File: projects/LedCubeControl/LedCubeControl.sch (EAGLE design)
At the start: 20 parts, among them IC1 74HC595N, IC2 74HC595N

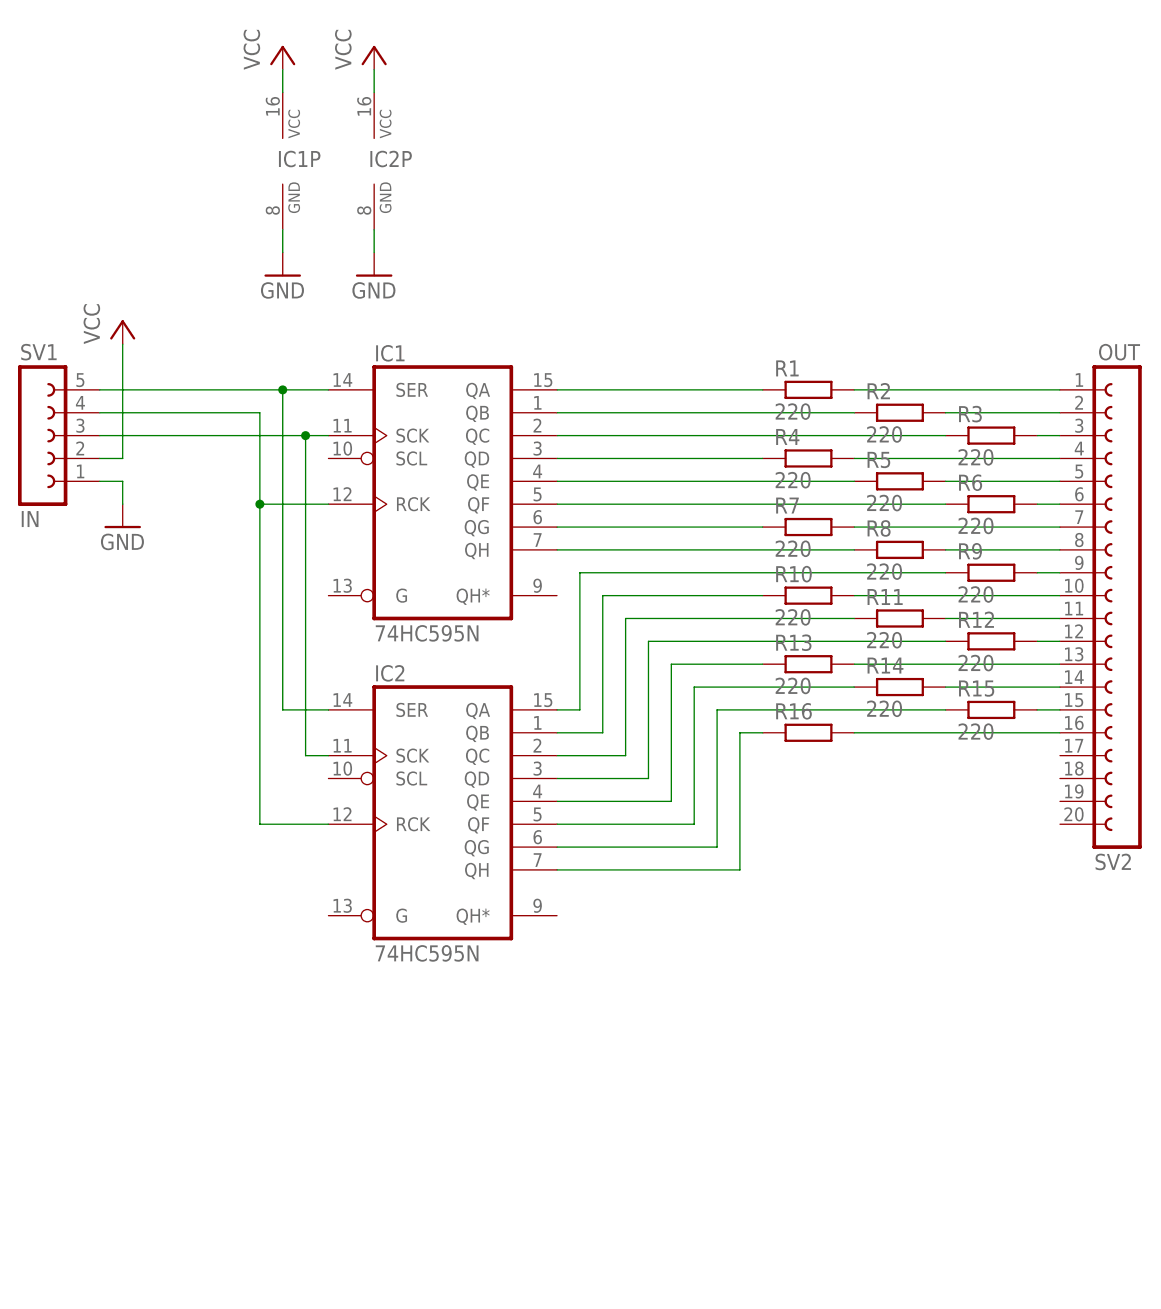
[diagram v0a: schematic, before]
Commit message: feat: led cube control
closes #9
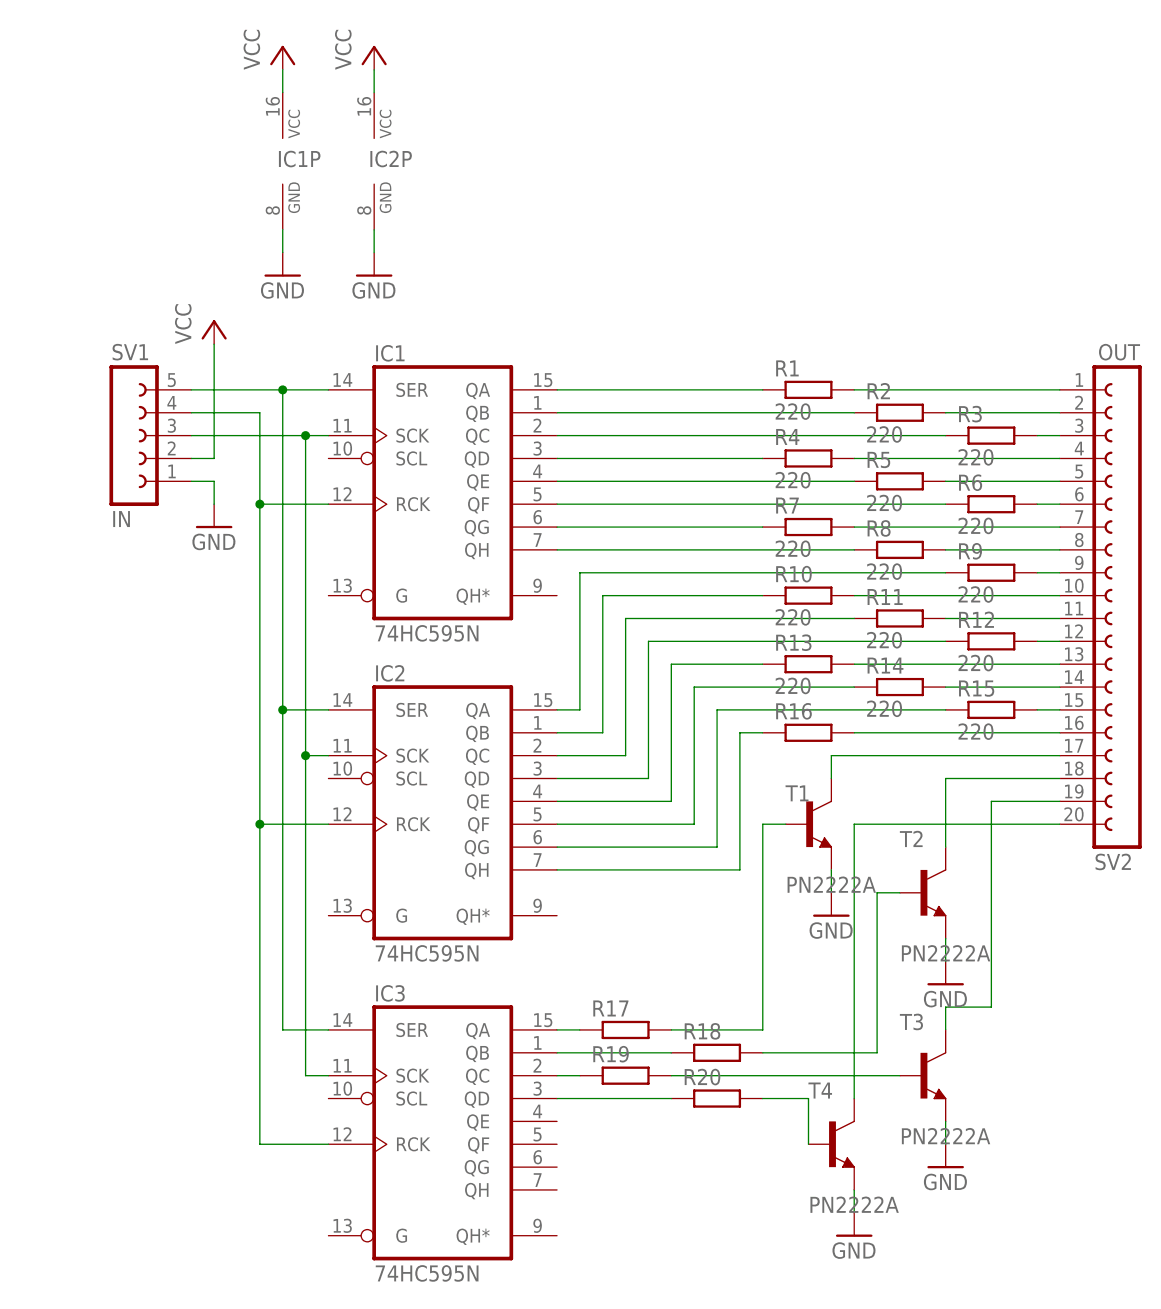
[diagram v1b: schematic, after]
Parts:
- added IC3: 74HC595N, 74xx-eu:74HC595N
- added R17, R18, R19, R20: 1k, rcl:R-EU_0207/10
- added T1, T2, T3, T4: PN2222A, transistor:BC317-NPN-TO92-EBC
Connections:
- new net N$36: IC3A.QA, R17.1
- new net N$37: R17.2, T1.B
- new net N$38: SV2.17, T1.C
- new net N$39: IC3A.QB, R18.1
- new net N$40: R18.2, T2.B
- new net N$41: SV2.18, T2.C
- new net N$42: IC3A.QC, R19.1
- new net N$43: SV2.19, T3.C
- new net N$44: R19.2, T3.B
- new net N$45: IC3A.QD, R20.1
- new net N$46: SV2.20, T4.C
- new net N$47: R20.2, T4.B
- net GND: now also T1.E, T2.E, T3.E, T4.E
- net N$1: now also IC3A.SCK
- net N$2: now also IC3A.SER
- net N$3: now also IC3A.RCK
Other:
- moved on the sheet: SV1

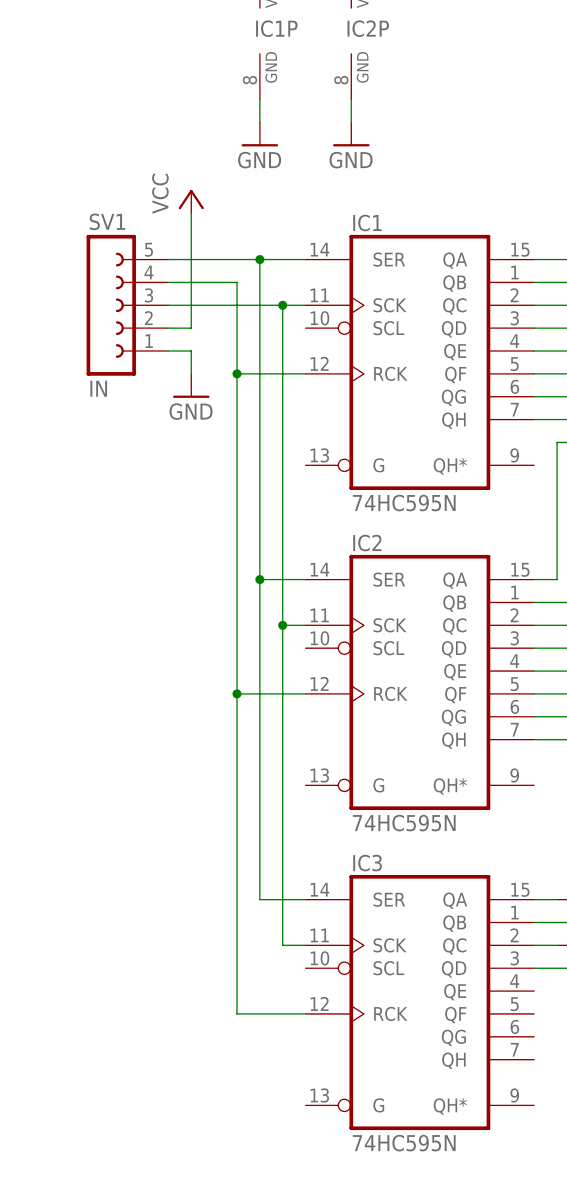
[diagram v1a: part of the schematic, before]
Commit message: fix: led cube drawimg fixed
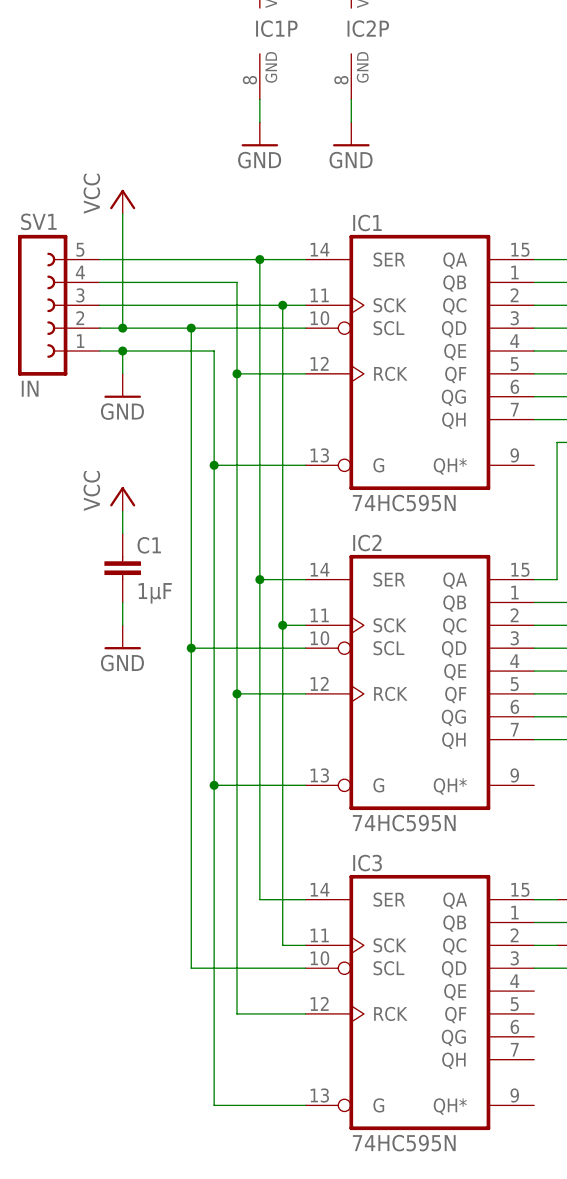
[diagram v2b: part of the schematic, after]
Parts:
- added C1: 1µF, rcl:C-EU050-024X044
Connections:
- net GND: now also C1.2, IC1A.G, IC2A.G, IC3A.G
- net VCC: now also C1.1, IC1A.SCL, IC2A.SCL, IC3A.SCL
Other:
- moved on the sheet: SV1
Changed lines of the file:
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@@
 <part name="GND7" library="supply1" library_urn="urn:adsk.eagle:library:371" deviceset="GND" device=""/>
 <part name="GND8" library="supply1" library_urn="urn:adsk.eagle:library:371" deviceset="GND" device=""/>
+<part name="P+4" library="supply1" library_urn="urn:adsk.eagle:library:371" deviceset="VCC" device=""/>
+<part name="GND4" library="supply1" library_urn="urn:adsk.eagle:library:371" deviceset="GND" device=""/>
+<part name="C1" library="rcl" library_urn="urn:adsk.eagle:library:334" deviceset="C-EU" device="050-024X044" package3d_urn="urn:adsk.eagle:package:23643/1" value="1µF"/>
 </parts>
 <sheets>
@@
 </plain>
 <instances>
-<instance part="SV1" gate="G$1" x="12.7" y="66.04" smashed="yes">
-<attribute name="VALUE" x="11.43" y="55.88" size="1.778" layer="96"/>
-<attribute name="NAME" x="11.43" y="74.422" size="1.778" layer="95"/>
+<instance part="SV1" gate="G$1" x="5.08" y="66.04" smashed="yes">
+<attribute name="VALUE" x="3.81" y="55.88" size="1.778" layer="96"/>
+<attribute name="NAME" x="3.81" y="74.422" size="1.778" layer="95"/>
 </instance>
 <instance part="R1" gate="G$1" x="88.9" y="71.12" smashed="yes">
@@
 <attribute name="NAME" x="85.09" y="34.5186" size="1.778" layer="95"/>
 </instance>
-<instance part="GND1" gate="1" x="22.86" y="55.88" smashed="yes">
-<attribute name="VALUE" x="20.32" y="53.34" size="1.778" layer="96"/>
+<instance part="GND1" gate="1" x="15.24" y="55.88" smashed="yes">
+<attribute name="VALUE" x="12.7" y="53.34" size="1.778" layer="96"/>
 </instance>
 <instance part="IC1" gate="P" x="30.48" y="96.52" smashed="yes">
@@
 <attribute name="VALUE" x="38.1" y="81.28" size="1.778" layer="96"/>
 </instance>
-<instance part="P+1" gate="VCC" x="22.86" y="78.74" smashed="yes">
-<attribute name="VALUE" x="20.32" y="76.2" size="1.778" layer="96" rot="R90"/>
+<instance part="P+1" gate="VCC" x="15.24" y="78.74" smashed="yes">
+<attribute name="VALUE" x="12.7" y="76.2" size="1.778" layer="96" rot="R90"/>
 </instance>
 <instance part="P+2" gate="VCC" x="30.48" y="109.22" smashed="yes">
@@
 <instance part="GND8" gate="1" x="91.44" y="12.7" smashed="yes">
 <attribute name="VALUE" x="88.9" y="10.16" size="1.778" layer="96"/>
+</instance>
+<instance part="P+4" gate="VCC" x="15.24" y="45.72" smashed="yes">
+<attribute name="VALUE" x="12.7" y="43.18" size="1.778" layer="96" rot="R90"/>
+</instance>
+<instance part="GND4" gate="1" x="15.24" y="27.94" smashed="yes">
+<attribute name="VALUE" x="12.7" y="25.4" size="1.778" layer="96"/>
+</instance>
+<instance part="C1" gate="G$1" x="15.24" y="38.1" smashed="yes">
+<attribute name="NAME" x="16.764" y="38.481" size="1.778" layer="95"/>
+<attribute name="VALUE" x="16.764" y="33.401" size="1.778" layer="96"/>
 </instance>
 </instances>
@@
 <wire x1="33.02" y1="66.04" x2="35.56" y2="66.04" width="0.1524" layer="91"/>
 <pinref part="SV1" gate="G$1" pin="3"/>
-<wire x1="20.32" y1="66.04" x2="33.02" y2="66.04" width="0.1524" layer="91"/>
+<wire x1="12.7" y1="66.04" x2="33.02" y2="66.04" width="0.1524" layer="91"/>
 <junction x="33.02" y="66.04"/>
 <pinref part="IC3" gate="A" pin="SCK"/>
@@
 <wire x1="30.48" y1="71.12" x2="35.56" y2="71.12" width="0.1524" layer="91"/>
 <pinref part="SV1" gate="G$1" pin="5"/>
-<wire x1="20.32" y1="71.12" x2="30.48" y2="71.12" width="0.1524" layer="91"/>
+<wire x1="12.7" y1="71.12" x2="30.48" y2="71.12" width="0.1524" layer="91"/>
 <junction x="30.48" y="71.12"/>
 <pinref part="IC3" gate="A" pin="SER"/>
@@
 <junction x="27.94" y="58.42"/>
 <pinref part="SV1" gate="G$1" pin="4"/>
-<wire x1="27.94" y1="68.58" x2="20.32" y2="68.58" width="0.1524" layer="91"/>
+<wire x1="27.94" y1="68.58" x2="12.7" y2="68.58" width="0.1524" layer="91"/>
 <pinref part="IC3" gate="A" pin="RCK"/>
 <wire x1="35.56" y1="-12.7" x2="27.94" y2="-12.7" width="0.1524" layer="91"/>
@@
 <segment>
 <pinref part="SV1" gate="G$1" pin="1"/>
-<wire x1="20.32" y1="60.96" x2="22.86" y2="60.96" width="0.1524" layer="91"/>
+<wire x1="12.7" y1="60.96" x2="15.24" y2="60.96" width="0.1524" layer="91"/>
 <pinref part="GND1" gate="1" pin="GND"/>
-<wire x1="22.86" y1="60.96" x2="22.86" y2="58.42" width="0.1524" layer="91"/>
+<wire x1="15.24" y1="60.96" x2="15.24" y2="58.42" width="0.1524" layer="91"/>
+<pinref part="IC1" gate="A" pin="G"/>
+<wire x1="35.56" y1="48.26" x2="25.4" y2="48.26" width="0.1524" layer="91"/>
+<wire x1="25.4" y1="48.26" x2="25.4" y2="60.96" width="0.1524" layer="91"/>
+<wire x1="25.4" y1="60.96" x2="15.24" y2="60.96" width="0.1524" layer="91"/>
+<junction x="15.24" y="60.96"/>
+<wire x1="25.4" y1="48.26" x2="25.4" y2="12.7" width="0.1524" layer="91"/>
+<junction x="25.4" y="48.26"/>
+<pinref part="IC2" gate="A" pin="G"/>
+<wire x1="25.4" y1="12.7" x2="35.56" y2="12.7" width="0.1524" layer="91"/>
+<wire x1="25.4" y1="12.7" x2="25.4" y2="-22.86" width="0.1524" layer="91"/>
+<junction x="25.4" y="12.7"/>
+<pinref part="IC3" gate="A" pin="G"/>
+<wire x1="25.4" y1="-22.86" x2="35.56" y2="-22.86" width="0.1524" layer="91"/>
 </segment>
 <segment>
@@
 <wire x1="104.14" y1="10.16" x2="104.14" y2="7.62" width="0.1524" layer="91"/>
 </segment>
+<segment>
+<pinref part="C1" gate="G$1" pin="2"/>
+<pinref part="GND4" gate="1" pin="GND"/>
+<wire x1="15.24" y1="33.02" x2="15.24" y2="30.48" width="0.1524" layer="91"/>
+</segment>
 </net>
 <net name="VCC" class="0">
 <segment>
 <pinref part="P+1" gate="VCC" pin="VCC"/>
-<wire x1="22.86" y1="76.2" x2="22.86" y2="63.5" width="0.1524" layer="91"/>
+<wire x1="15.24" y1="76.2" x2="15.24" y2="63.5" width="0.1524" layer="91"/>
 <pinref part="SV1" gate="G$1" pin="2"/>
-<wire x1="22.86" y1="63.5" x2="20.32" y2="63.5" width="0.1524" layer="91"/>
+<wire x1="15.24" y1="63.5" x2="12.7" y2="63.5" width="0.1524" layer="91"/>
+<pinref part="IC3" gate="A" pin="SCL"/>
+<wire x1="35.56" y1="-7.62" x2="22.86" y2="-7.62" width="0.1524" layer="91"/>
+<wire x1="22.86" y1="-7.62" x2="22.86" y2="27.94" width="0.1524" layer="91"/>
+<wire x1="22.86" y1="27.94" x2="22.86" y2="63.5" width="0.1524" layer="91"/>
+<wire x1="22.86" y1="63.5" x2="15.24" y2="63.5" width="0.1524" layer="91"/>
+<junction x="15.24" y="63.5"/>
+<pinref part="IC2" gate="A" pin="SCL"/>
+<wire x1="35.56" y1="27.94" x2="22.86" y2="27.94" width="0.1524" layer="91"/>
+<junction x="22.86" y="27.94"/>
+<pinref part="IC1" gate="A" pin="SCL"/>
+<wire x1="35.56" y1="63.5" x2="22.86" y2="63.5" width="0.1524" layer="91"/>
+<junction x="22.86" y="63.5"/>
 </segment>
 <segment>
@@
 <pinref part="IC2" gate="P" pin="VCC"/>
 <wire x1="40.64" y1="106.68" x2="40.64" y2="104.14" width="0.1524" layer="91"/>
+</segment>
+<segment>
+<pinref part="C1" gate="G$1" pin="1"/>
+<pinref part="P+4" gate="VCC" pin="VCC"/>
+<wire x1="15.24" y1="40.64" x2="15.24" y2="43.18" width="0.1524" layer="91"/>
 </segment>
 </net>
@@
 </sheet>
 </sheets>
-<errors>
-</errors>
 </schematic>
 </drawing>

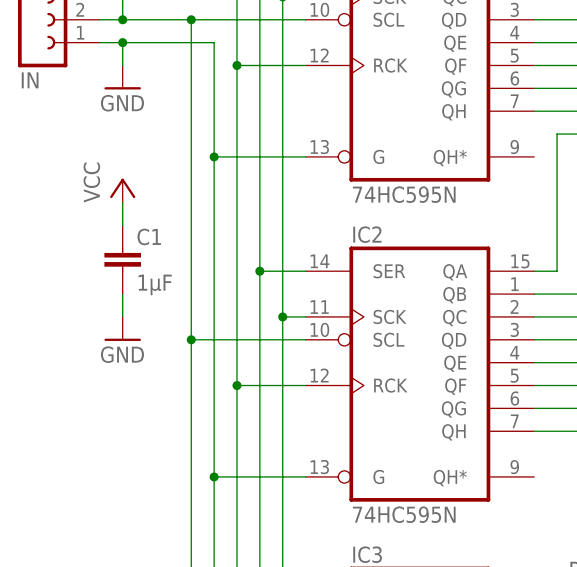
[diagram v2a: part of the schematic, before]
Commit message: fix: capacitor value fixed
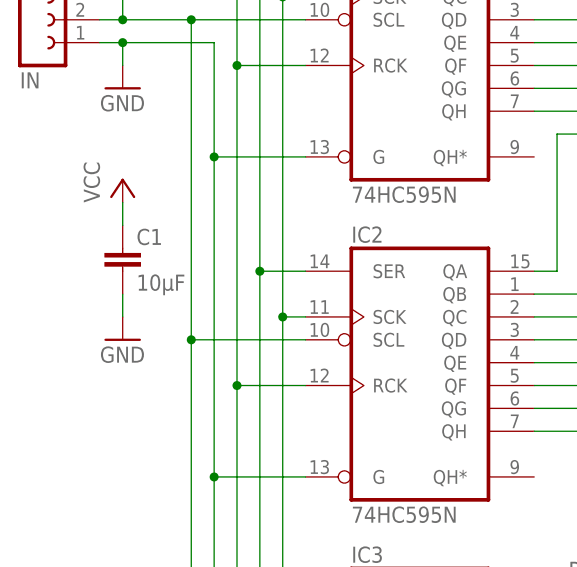
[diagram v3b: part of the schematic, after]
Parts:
- C1: value 1µF -> 10µF
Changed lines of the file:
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@@
 <part name="P+4" library="supply1" library_urn="urn:adsk.eagle:library:371" deviceset="VCC" device=""/>
 <part name="GND4" library="supply1" library_urn="urn:adsk.eagle:library:371" deviceset="GND" device=""/>
-<part name="C1" library="rcl" library_urn="urn:adsk.eagle:library:334" deviceset="C-EU" device="050-024X044" package3d_urn="urn:adsk.eagle:package:23643/1" value="1µF"/>
+<part name="C1" library="rcl" library_urn="urn:adsk.eagle:library:334" deviceset="C-EU" device="050-024X044" package3d_urn="urn:adsk.eagle:package:23643/1" value="10µF"/>
 </parts>
 <sheets>
